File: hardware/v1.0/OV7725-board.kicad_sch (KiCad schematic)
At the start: 15 parts, among them J10 Conn_01x34, J11 Conn_02x10_Odd_Even, J8 Conn_01x04, U10 TLV62585

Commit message: backup
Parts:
- removed D6: LED, LED_SMD:LED_0805_2012Metric, symbol Device:LED
- removed R25, R26: 270, Resistor_SMD:R_0603_1608Metric, symbol Device:R_Small
- added C38: 10nf, Capacitor_SMD:C_0603_1608Metric, symbol Device:C_Small
- added R28, R29: 4.7K, Resistor_SMD:R_0603_1608Metric, symbol Device:R_Small
- added R33: 20, Resistor_SMD:R_0603_1608Metric, symbol Device:R_Small
- added RN17, RN18, RN19, RN20: 0, Resistor_SMD:R_Array_Convex_4x0603, symbol Device:R_Pack04
- added Y2: TFOM24M4RHKCNT2T, symbol mylib:TFOM24M4RHKCNT2T
- J13: renamed from J11; footprint Connector_PinHeader_2.54mm:PinHeader_2x10_P2.54mm_Vertical -> Connector_PinSocket_2.54mm:PinSocket_2x10_P2.54mm_Vertical
- renumbered C38 to C39, D5 to D3, J8 to J11, J10 to J12, R24 to R30, R27 to R31, R28 to R32, U10 to U11
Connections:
- net PWDN is gone; now on net GND: J13.18 (Pin_18)
- net +3V3: now also C38.1, R28.1, R29.1, Y2.1 (OE), Y2.4 (VCC)
- net GND: now also C38.2, Y2.2 (GND)
- net OV7725_CLK: now also RN17.5 (R4.2); no longer J12.2 (Pin_2)
- net OV7725_HS: now also RN17.6 (R3.2); no longer J12.3 (Pin_3)
- net OV7725_P0: now also RN18.7 (R2.2); no longer J12.20 (Pin_20)
- net OV7725_P1: now also RN18.8 (R1.2); no longer J12.21 (Pin_21)
- net OV7725_P2: now also RN19.5 (R4.2); no longer J12.22 (Pin_22)
- net OV7725_P3: now also RN19.6 (R3.2); no longer J12.23 (Pin_23)
- net OV7725_P4: now also RN19.7 (R2.2); no longer J12.24 (Pin_24)
- net OV7725_P5: now also RN19.8 (R1.2); no longer J12.25 (Pin_25)
- net OV7725_P6: now also RN20.5 (R4.2); no longer J12.26 (Pin_26)
- net OV7725_P7: now also RN20.6 (R3.2); no longer J12.27 (Pin_27)
- net OV7725_P8: now also RN20.7 (R2.2); no longer J12.28 (Pin_28)
- net OV7725_P9: now also RN20.8 (R1.2); no longer J12.29 (Pin_29)
- net OV7725_VS: now also RN17.8 (R1.2); no longer J12.5 (Pin_5)
- net SCLK: now also R29.2
- net SDATA: now also R28.2
- net XCLK: now also R33.2
- new net: R33.1, Y2.3 (OUT)
- new net: J12.29 (Pin_29), RN20.1 (R1.1)
- new net: J12.28 (Pin_28), RN20.2 (R2.1)
- new net: J12.27 (Pin_27), RN20.3 (R3.1)
- new net: J12.26 (Pin_26), RN20.4 (R4.1)
- new net: J12.5 (Pin_5), RN17.1 (R1.1)
- new net: J12.3 (Pin_3), RN17.3 (R3.1)
- new net: J12.2 (Pin_2), RN17.4 (R4.1)
- new net: J12.20 (Pin_20), RN18.2 (R2.1)
- new net: J12.21 (Pin_21), RN18.1 (R1.1)
- new net: J12.22 (Pin_22), RN19.4 (R4.1)
- new net: J12.23 (Pin_23), RN19.3 (R3.1)
- new net: J12.24 (Pin_24), RN19.2 (R2.1)
- new net: J12.25 (Pin_25), RN19.1 (R1.1)
- no-connect marks 16 -> 22
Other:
- note added: "Normal mode"
- note added: "OSCILLATOR"
- moved on the sheet: J11, J12

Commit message: changes
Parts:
- added C41: 0.1uf, Capacitor_SMD:C_0603_1608Metric, symbol Device:C_Small
- added TP4: VCC_PAD, TestPoint:TestPoint_Pad_D1.5mm, symbol Connector:TestPoint_Flag
- added TP5: SWIO_PAD, TestPoint:TestPoint_Pad_D1.5mm, symbol Connector:TestPoint_Flag
- added TP6: GND_PAD, TestPoint:TestPoint_Pad_D1.5mm, symbol Connector:TestPoint_Flag
- added U12: CH32V003JxMx, Package_SO:SOP-8_3.9x4.9mm_P1.27mm, symbol MCU_WCH_CH32V0:CH32V003JxMx
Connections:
- net +3V3: now also C41.1, TP4.1, U12.4 (VDD)
- net GND: now also C41.2, TP6.1, U12.2 (VSS)
- net RST: now also U12.7 (PC4)
- net SCLK: now also U12.6 (PC2)
- net SDATA: now also U12.5 (PC1)
- new net SWIO: TP5.1, U12.8 (PD1/PD4/PD5)
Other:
- note added: "MCU"

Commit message: changes
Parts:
- R31, R32: footprint Resistor_SMD:R_0402_1005Metric -> Resistor_SMD:R_0603_1608Metric
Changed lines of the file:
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@@
 			)
 		)
-		(property "Footprint" "Resistor_SMD:R_0402_1005Metric"
+		(property "Footprint" "Resistor_SMD:R_0603_1608Metric"
 			(at 141.605 34.925 0)
 			(effects
@@
 			)
 		)
-		(property "Footprint" "Resistor_SMD:R_0402_1005Metric"
+		(property "Footprint" "Resistor_SMD:R_0603_1608Metric"
 			(at 141.605 28.575 0)
 			(effects

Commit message: backup
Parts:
- removed C37: 22uf, Capacitor_SMD:C_0805_2012Metric, symbol Device:C_Small
- C36: value 22uf -> 4.7uf
- C39: value 22uf -> 10uf
- L3: value 1uh -> 2.2uh
- R28, R29: value 4.7K -> 4.7k
- R31: value 450K -> 450k
- R32: value 100K -> 100k
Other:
- moved on the sheet: C36, C39, C41, L3, R31, R32, TP4, TP5, TP6, U11, U12

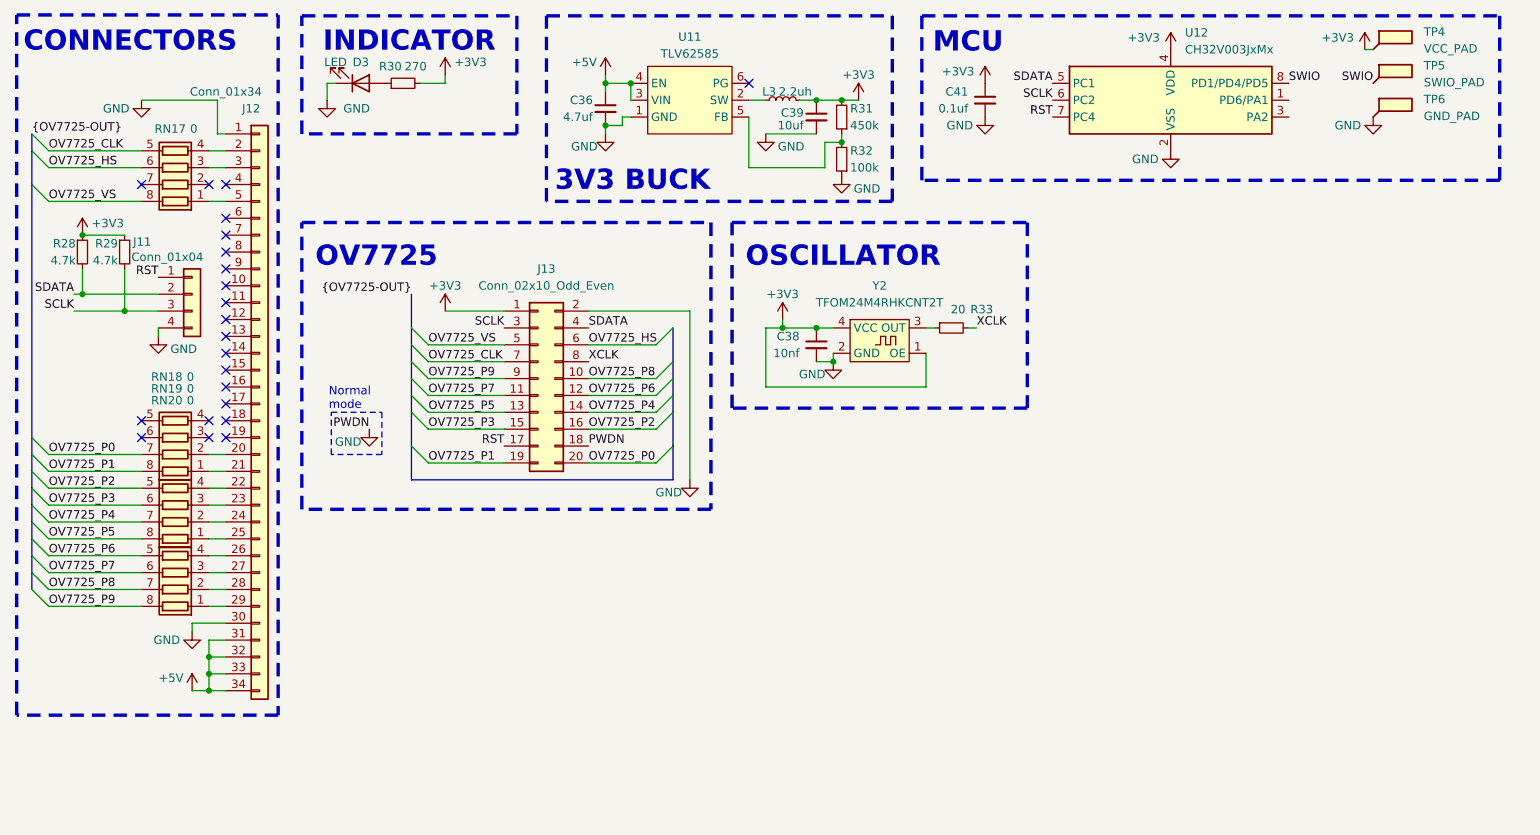
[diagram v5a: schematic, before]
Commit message: added pmod connectors instead of leds
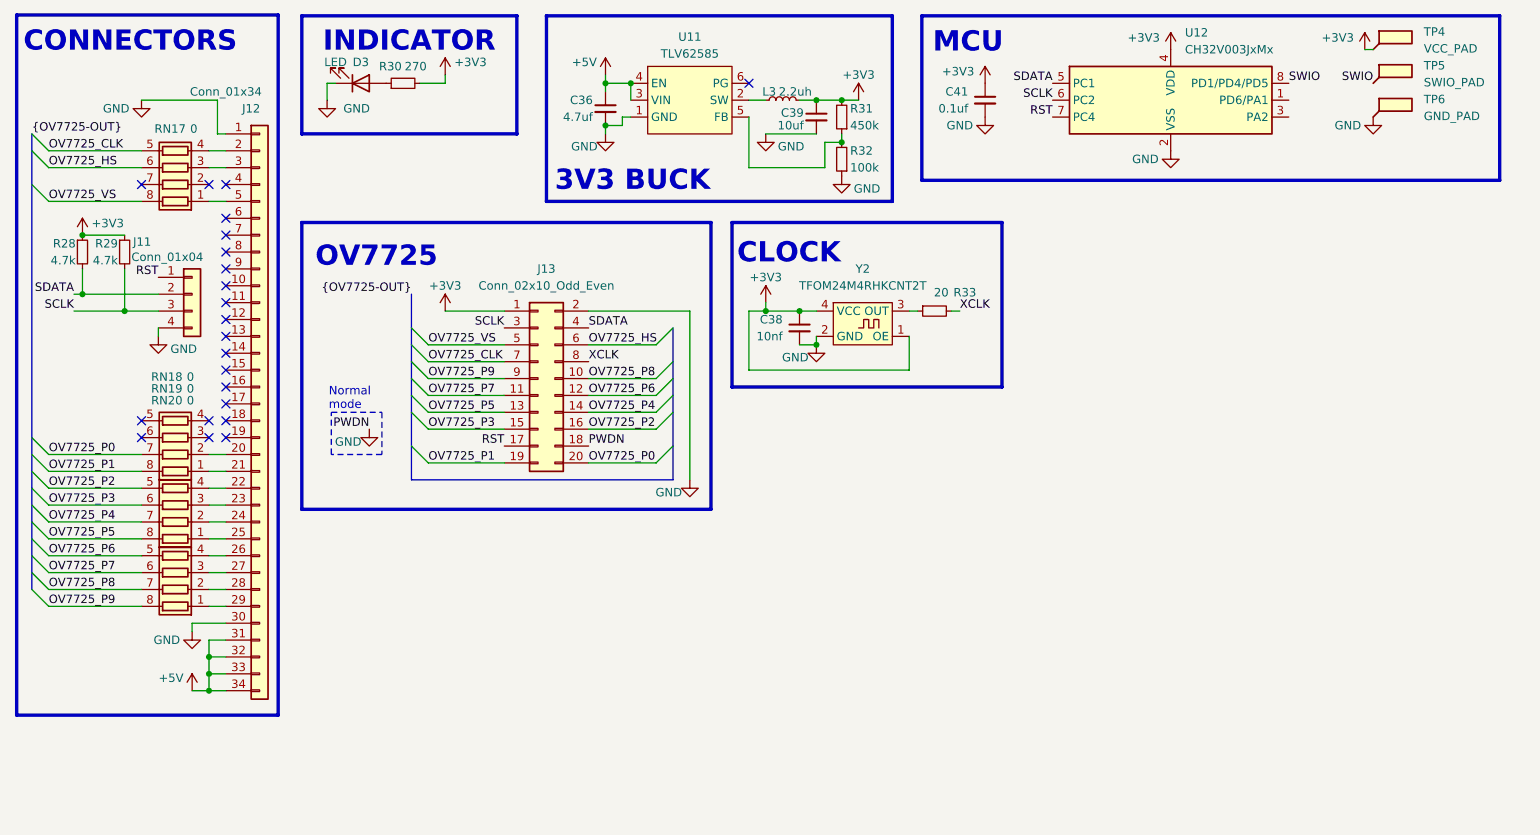
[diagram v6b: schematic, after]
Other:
- note added: "CLOCK"
- note removed: "OSCILLATOR"
- moved on the sheet: C38, R33, Y2
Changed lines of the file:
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@@
 	(rectangle
 		(start 121.92 45.085)
-		(end 166.37 73.025)
+		(end 162.56 69.85)
 		(stroke
 			(width 0.508)
-			(type dash)
+			(type solid)
 		)
 		(fill
@@
 		(stroke
 			(width 0.508)
-			(type dash)
+			(type solid)
 		)
 		(fill
@@
 		(stroke
 			(width 0.508)
-			(type dash)
+			(type solid)
 		)
 		(fill
@@
 		(stroke
 			(width 0.508)
-			(type dash)
+			(type solid)
 		)
 		(fill
@@
 		(stroke
 			(width 0.508)
-			(type dash)
+			(type solid)
 		)
 		(fill
@@
 		(stroke
 			(width 0.508)
-			(type dash)
+			(type solid)
 		)
 		(fill
@@
 		)
 	)
-	(text "OSCILLATOR"
+	(text "CLOCK"
 		(exclude_from_sim no)
-		(at 123.952 52.07 0)
+		(at 122.682 51.562 0)
 		(effects
 			(font
@@
 	)
 	(junction
-		(at 134.62 60.96)
+		(at 132.08 58.42)
 		(diameter 0)
 		(color 0 0 0 0)
@@
 	)
 	(junction
-		(at 129.54 60.96)
+		(at 127 58.42)
 		(diameter 0)
 		(color 0 0 0 0)
@@
 	)
 	(junction
-		(at 137.16 66.04)
+		(at 134.62 63.5)
 		(diameter 0)
 		(color 0 0 0 0)
@@
 	(wire
 		(pts
-			(xy 158.75 60.96) (xy 157.48 60.96)
+			(xy 156.21 58.42) (xy 154.94 58.42)
 		)
 		(stroke
@@
 	(wire
 		(pts
-			(xy 151.13 69.85) (xy 127 69.85)
+			(xy 148.59 67.31) (xy 124.46 67.31)
 		)
 		(stroke
@@
 	(wire
 		(pts
-			(xy 134.62 66.04) (xy 137.16 66.04)
+			(xy 132.08 63.5) (xy 134.62 63.5)
 		)
 		(stroke
@@
 	(wire
 		(pts
-			(xy 127 69.85) (xy 127 60.96)
+			(xy 124.46 67.31) (xy 124.46 58.42)
 		)
 		(stroke
@@
 	(wire
 		(pts
-			(xy 151.13 64.77) (xy 151.13 69.85)
+			(xy 148.59 62.23) (xy 148.59 67.31)
 		)
 		(stroke
@@
 	(wire
 		(pts
-			(xy 134.62 60.96) (xy 137.16 60.96)
+			(xy 132.08 58.42) (xy 134.62 58.42)
 		)
 		(stroke
@@
 	(wire
 		(pts
-			(xy 129.54 60.96) (xy 134.62 60.96)
+			(xy 127 58.42) (xy 132.08 58.42)
 		)
 		(stroke
@@
 	(wire
 		(pts
-			(xy 129.54 59.69) (xy 129.54 60.96)
+			(xy 127 57.15) (xy 127 58.42)
 		)
 		(stroke
@@
 	(wire
 		(pts
-			(xy 137.16 66.04) (xy 137.16 64.77)
+			(xy 134.62 63.5) (xy 134.62 62.23)
 		)
 		(stroke
@@
 	(wire
 		(pts
-			(xy 151.13 60.96) (xy 152.4 60.96)
+			(xy 148.59 58.42) (xy 149.86 58.42)
 		)
 		(stroke
@@
 	(wire
 		(pts
-			(xy 127 60.96) (xy 129.54 60.96)
+			(xy 124.46 58.42) (xy 127 58.42)
 		)
 		(stroke
@@
 	)
 	(label "XCLK"
-		(at 158.75 60.96 0)
+		(at 156.21 58.42 0)
 		(effects
 			(font
@@
 	(symbol
 		(lib_id "power:+3V3")
-		(at 129.54 59.69 0)
+		(at 127 57.15 0)
 		(unit 1)
 		(exclude_from_sim no)
@@
 		(dnp no)
 		(property "Reference" "#PWR97"
-			(at 129.54 63.5 0)
+			(at 127 60.96 0)
 			(effects
 				(font
@@
 		)
 		(property "Value" "+3V3"
-			(at 129.54 55.88 0)
+			(at 127 53.34 0)
 			(effects
 				(font
@@
 		)
 		(property "Footprint" ""
-			(at 129.54 59.69 0)
+			(at 127 57.15 0)
 			(effects
 				(font
@@
 		)
 		(property "Datasheet" ""
-			(at 129.54 59.69 0)
+			(at 127 57.15 0)
 			(effects
 				(font
@@
 		)
 		(property "Description" "Power symbol creates a global label with name \"+3V3\""
-			(at 129.54 59.69 0)
+			(at 127 57.15 0)
 			(effects
 				(font
@@
 	(symbol
 		(lib_id "Device:R_Small")
-		(at 154.94 60.96 90)
+		(at 152.4 58.42 90)
 		(mirror x)
 		(unit 1)
@@
 		(dnp no)
 		(property "Reference" "R33"
-			(at 159.512 58.166 90)
+			(at 156.972 55.626 90)
 			(effects
 				(font
@@
 		)
 		(property "Value" "20"
-			(at 155.956 58.166 90)
+			(at 153.416 55.626 90)
 			(effects
 				(font
@@
 		)
 		(property "Footprint" "Resistor_SMD:R_0603_1608Metric"
-			(at 154.94 60.96 0)
+			(at 152.4 58.42 0)
 			(effects
 				(font
@@
 		)
 		(property "Datasheet" "~"
-			(at 154.94 60.96 0)
+			(at 152.4 58.42 0)
 			(effects
 				(font
@@
 		)
 		(property "Description" "Resistor, small symbol"
-			(at 154.94 60.96 0)
+			(at 152.4 58.42 0)
 			(effects
 				(font
@@
 	(symbol
 		(lib_id "Device:C_Small")
-		(at 134.62 63.5 0)
+		(at 132.08 60.96 0)
 		(unit 1)
 		(exclude_from_sim no)
@@
 		(dnp no)
 		(property "Reference" "C38"
-			(at 132.08 62.2362 0)
+			(at 129.54 59.6962 0)
 			(effects
 				(font
@@
 		)
 		(property "Value" "10nf"
-			(at 132.08 64.7762 0)
+			(at 129.54 62.2362 0)
 			(effects
 				(font
@@
 		)
 		(property "Footprint" "Capacitor_SMD:C_0603_1608Metric"
-			(at 134.62 63.5 0)
+			(at 132.08 60.96 0)
 			(effects
 				(font
@@
 		)
 		(property "Datasheet" "~"
-			(at 134.62 63.5 0)
+			(at 132.08 60.96 0)
 			(effects
 				(font
@@
 		)
 		(property "Description" "Unpolarized capacitor, small symbol"
-			(at 134.62 63.5 0)
+			(at 132.08 60.96 0)
 			(effects
 				(font
@@
 	(symbol
 		(lib_id "mylib:TFOM24M4RHKCNT2T")
-		(at 144.78 63.5 0)
+		(at 142.24 60.96 0)
 		(unit 1)
 		(exclude_from_sim no)
@@
 		(fields_autoplaced yes)
 		(property "Reference" "Y2"
-			(at 144.145 54.61 0)
+			(at 141.605 52.07 0)
 			(effects
 				(font
@@
 		)
 		(property "Value" "TFOM24M4RHKCNT2T"
-			(at 144.145 57.15 0)
+			(at 141.605 54.61 0)
 			(effects
 				(font
@@
 		)
 		(property "Footprint" ""
-			(at 144.78 63.5 0)
+			(at 142.24 60.96 0)
 			(effects
 				(font
@@
 		)
 		(property "Datasheet" "https://www.lcsc.com/datasheet/lcsc_datasheet_2410010301_Yajingxin-TFOM24M4RHKCNT2T_C454612.pdf"
-			(at 144.78 53.086 0)
+			(at 142.24 50.546 0)
 			(show_name yes)
 			(effects
@@
 		)
 		(property "Description" ""
-			(at 144.78 63.5 0)
+			(at 142.24 60.96 0)
 			(effects
 				(font
@@
 	(symbol
 		(lib_id "power:GND")
-		(at 137.16 66.04 0)
+		(at 134.62 63.5 0)
 		(unit 1)
 		(exclude_from_sim no)
@@
 		(dnp no)
 		(property "Reference" "#PWR99"
-			(at 137.16 72.39 0)
+			(at 134.62 69.85 0)
 			(effects
 				(font
@@
 		)
 		(property "Value" "GND"
-			(at 133.985 67.945 0)
+			(at 131.445 65.405 0)
 			(effects
 				(font
@@
 		)
 		(property "Footprint" ""
-			(at 137.16 66.04 0)
+			(at 134.62 63.5 0)
 			(effects
 				(font
@@
 		)
 		(property "Datasheet" ""
-			(at 137.16 66.04 0)
+			(at 134.62 63.5 0)
 			(effects
 				(font
@@
 		)
 		(property "Description" "Power symbol creates a global label with name \"GND\" , ground"
-			(at 137.16 66.04 0)
+			(at 134.62 63.5 0)
 			(effects
 				(font

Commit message: first schematic iteration done
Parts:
- removed D3: LED, LED_SMD:LED_0805_2012Metric, symbol Device:LED
- removed R28, R29: 4.7k, Resistor_SMD:R_0603_1608Metric, symbol Device:R_Small
- removed R30: 270, Resistor_SMD:R_0603_1608Metric, symbol Device:R_Small
- added D4: ~, C779813:LED-SMD_4P-L1.6-W1.5-BR_TZ-P4-1615, symbol Device:LED_ARGB
- added R42: 4.7k, Resistor_SMD:R_0603_1608Metric, symbol Device:R_Small
- added RN23: 5.1k, symbol Device:R_Pack02
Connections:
- net +3V3: now also J13.19 (Pin_19), R42.2, RN23.3 (R2.2), RN23.4 (R1.2); no longer J13.1 (Pin_1)
- net GND: now also J13.20 (Pin_20), J13.4 (Pin_4), D4.2 (RK); no longer J13.18 (Pin_18), J13.2 (Pin_2)
- net OV7725_CLK: now also J13.13 (Pin_13); no longer J13.7 (Pin_7)
- net OV7725_HS: now also J13.16 (Pin_16); no longer J13.6 (Pin_6)
- net OV7725_P0: now also J13.2 (Pin_2); no longer J13.20 (Pin_20)
- net OV7725_P1: now also J13.1 (Pin_1); no longer J13.19 (Pin_19)
- net OV7725_P2: now also J13.6 (Pin_6); no longer J13.16 (Pin_16)
- net OV7725_P3: now also J13.5 (Pin_5); no longer J13.15 (Pin_15)
- net OV7725_P4: now also J13.8 (Pin_8); no longer J13.14 (Pin_14)
- net OV7725_P5: now also J13.7 (Pin_7); no longer J13.13 (Pin_13)
- net OV7725_P6: now also J13.10 (Pin_10); no longer J13.12 (Pin_12)
- net OV7725_P7: now also J13.9 (Pin_9); no longer J13.11 (Pin_11)
- net OV7725_P8: now also J13.12 (Pin_12); no longer J13.10 (Pin_10)
- net OV7725_P9: now also J13.11 (Pin_11); no longer J13.9 (Pin_9)
- net OV7725_VS: now also J13.15 (Pin_15); no longer J13.5 (Pin_5)
- net RST: now also J13.3 (Pin_3); no longer J13.17 (Pin_17)
- net SCLK: now also J13.17 (Pin_17), RN23.2 (R2.1); no longer J13.3 (Pin_3)
- net SDATA: now also J13.18 (Pin_18), RN23.1 (R1.1); no longer J13.4 (Pin_4)
- net XCLK: now also J13.14 (Pin_14); no longer J13.8 (Pin_8)
- new net: D4.1 (A), R42.1
- new net STATUS: D4.3 (GK)
- no-connect marks 22 -> 23

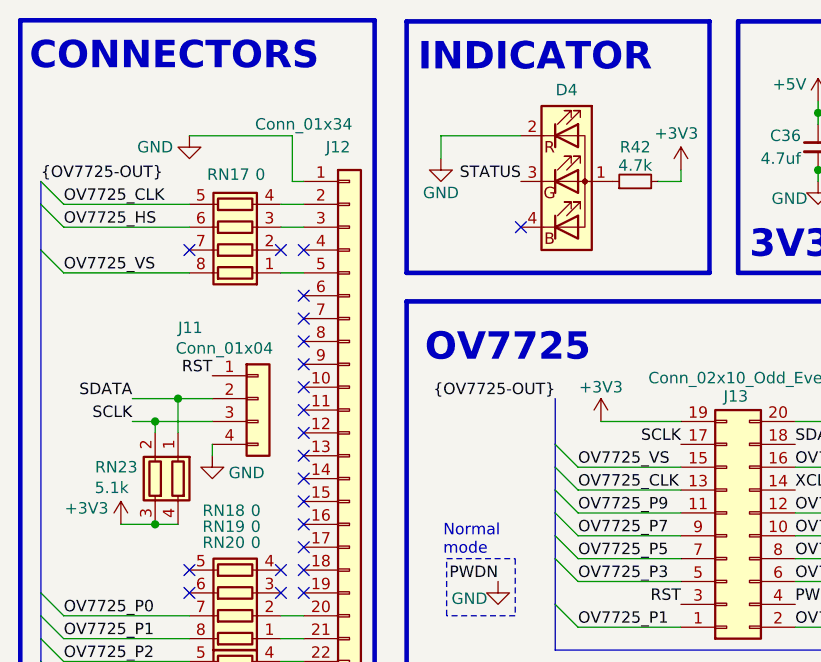
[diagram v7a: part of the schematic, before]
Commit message: did PORT0 routing
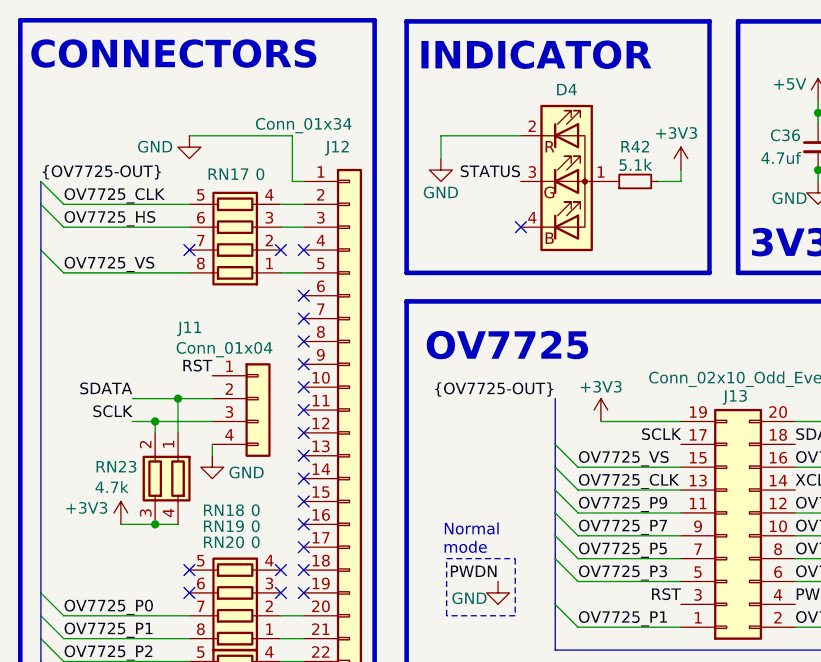
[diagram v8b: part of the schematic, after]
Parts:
- R42: value 4.7k -> 5.1k
- RN23: value 5.1k -> 4.7k; footprint (none) -> Resistor_SMD:R_Array_Convex_2x0603
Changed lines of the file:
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@@
 			)
 		)
-		(property "Value" "5.1k"
+		(property "Value" "4.7k"
 			(at 24.384 65.786 0)
 			(effects
@@
 			)
 		)
-		(property "Footprint" ""
+		(property "Footprint" "Resistor_SMD:R_Array_Convex_2x0603"
 			(at 24.765 64.77 90)
 			(effects
@@
 			)
 		)
-		(property "Value" "4.7k"
+		(property "Value" "5.1k"
 			(at 82.55 29.972 90)
 			(effects
